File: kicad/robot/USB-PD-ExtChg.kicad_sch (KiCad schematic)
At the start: 28 parts, among them J1 USBC_Receptacle_SMD_RA, Q3 YJL3416A, Q4 YJL3416A, U18 AP33771DKZ-13, U25 TVS0500DRV, U26 TPD1E05U06, U27 TPD1E05U06

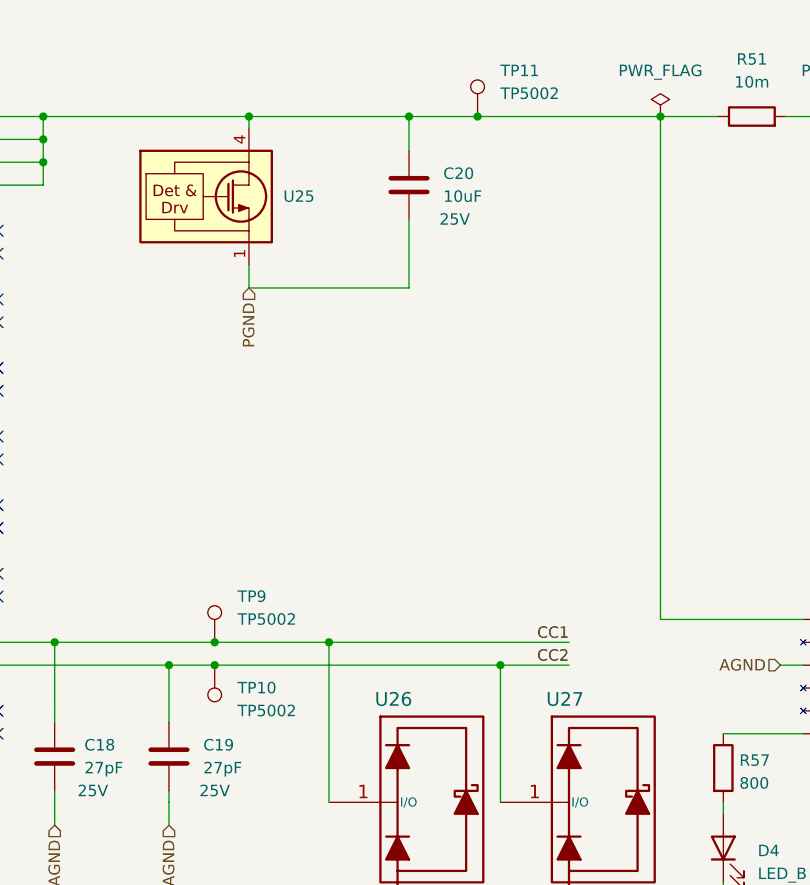
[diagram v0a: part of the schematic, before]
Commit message: Hide all test point values keep ref
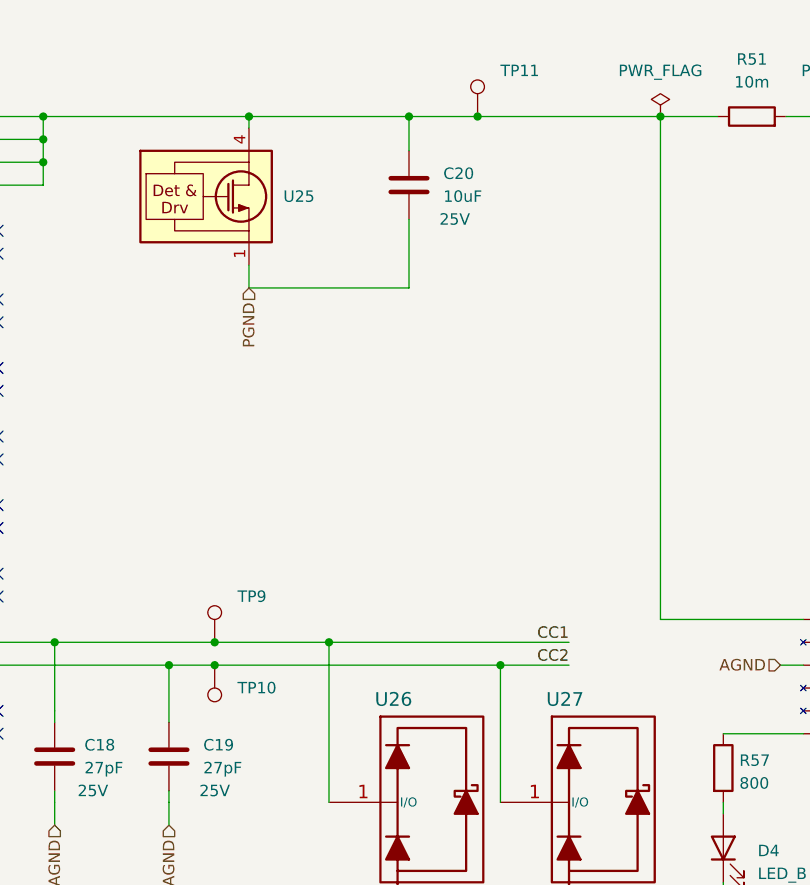
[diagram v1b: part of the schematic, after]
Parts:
- TP10, TP11, TP9: value TP5002 -> TestPoint
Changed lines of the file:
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@@
       (effects (font (size 1.27 1.27)) (justify left))
     )
-    (property "Value" "TP5002" (at 209.55 181.61 0)
-      (effects (font (size 1.27 1.27)) (justify left))
+    (property "Value" "TestPoint" (at 209.55 181.61 0)
+      (effects (font (size 1.27 1.27)) (justify left) hide)
     )
     (property "Footprint" "TestPoint:KEYSTONE_5002" (at 212.09 184.15 0)
@@
       (effects (font (size 1.27 1.27)) (justify left))
     )
-    (property "Value" "TP5002" (at 238.76 123.19 0)
-      (effects (font (size 1.27 1.27)) (justify left))
+    (property "Value" "TestPoint" (at 238.76 123.19 0)
+      (effects (font (size 1.27 1.27)) (justify left) hide)
     )
     (property "Footprint" "TestPoint:KEYSTONE_5002" (at 241.3 125.73 0)
@@
       (effects (font (size 1.27 1.27)) (justify right))
     )
-    (property "Value" "TP5002" (at 209.55 191.77 0)
-      (effects (font (size 1.27 1.27)) (justify right))
+    (property "Value" "TestPoint" (at 209.55 191.77 0)
+      (effects (font (size 1.27 1.27)) (justify right) hide)
     )
     (property "Footprint" "TestPoint:KEYSTONE_5002" (at 201.93 186.69 0)

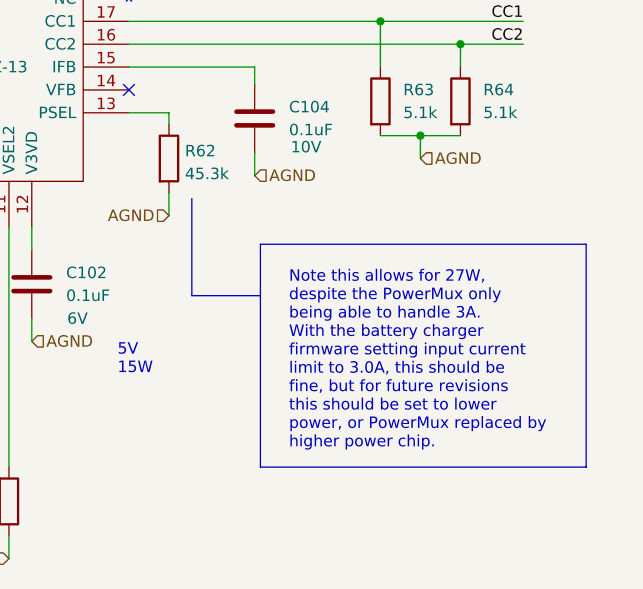
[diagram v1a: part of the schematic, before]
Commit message: Swap out R62 from 45.3k to 16k
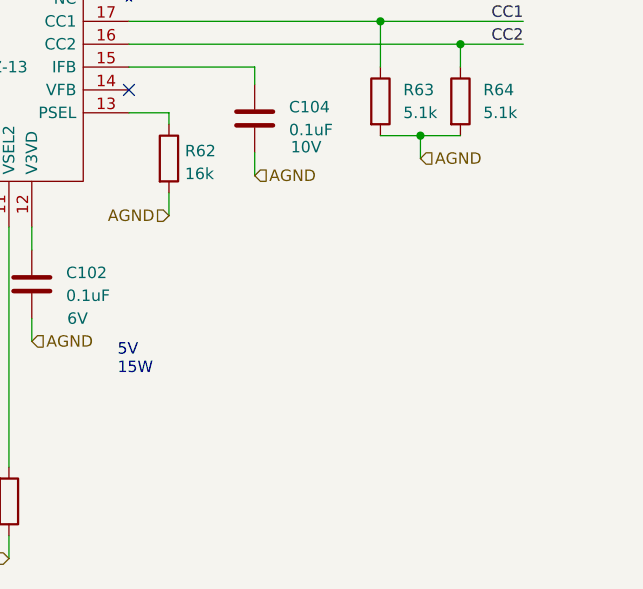
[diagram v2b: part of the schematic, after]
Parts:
- R62: value 45.3k -> 16k; Manufacturer Stackpole Electronics -> (none); Part Number RMCF0603FT45K3 -> (none)
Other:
- note removed: "Note this allows for 27W, despite the PowerMux only being able to handle 3A. With the battery charger firmware setting input current limit to 3.0A, this should be fine, but for future revisions this should be set to lower power, or PowerMux replaced by higher power chip."
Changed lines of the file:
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@@
-    (stroke (width 0) (type default))
-  )
-  (polyline (pts (xy 360.045 233.68) (xy 323.85 233.68))
     (stroke (width 0) (type default))
   )
@@
     (stroke (width 0) (type default))
   )
-  (polyline (pts (xy 323.85 208.915) (xy 360.045 208.915))
-    (stroke (width 0) (type default))
-  )
   (wire (pts (xy 187.96 125.73) (xy 210.82 125.73))
     (stroke (width 0) (type default))
@@
     (stroke (width 0) (type default))
   )
-  (polyline (pts (xy 360.045 208.915) (xy 360.045 233.68))
-    (stroke (width 0) (type default))
-  )
   (wire (pts (xy 263.525 194.31) (xy 272.415 194.31))
     (stroke (width 0) (type default))
@@
     (stroke (width 0) (type default))
   )
-  (polyline (pts (xy 323.85 214.63) (xy 323.85 233.68))
-    (stroke (width 0) (type default))
-  )
   (wire (pts (xy 187.96 133.35) (xy 187.96 130.81))
     (stroke (width 0.254) (type default))
@@
     (stroke (width 0) (type default))
   )
-  (polyline (pts (xy 316.23 203.835) (xy 316.23 214.63))
-    (stroke (width 0) (type default))
-  )
   (wire (pts (xy 228.6 125.73) (xy 228.6 129.54))
     (stroke (width 0) (type default))
@@
     (stroke (width 0.254) (type default))
   )
-  (polyline (pts (xy 323.85 214.63) (xy 323.85 208.915))
-    (stroke (width 0) (type default))
-  )
   (wire (pts (xy 189.23 184.15) (xy 207.01 184.15))
     (stroke (width 0.254) (type default))
@@
     (stroke (width 0) (type default))
   )
-  (polyline (pts (xy 316.23 214.63) (xy 323.85 214.63))
-    (stroke (width 0) (type default))
-  )
   (wire (pts (xy 210.82 125.73) (xy 210.82 127))
     (stroke (width 0) (type default))
@@
   )
   (text "5V\n15W" (at 307.975 223.52 0)
-    (effects (font (size 1.27 1.27)) (justify left bottom))
-  )
-  (text "Note this allows for 27W, \ndespite the PowerMux only\nbeing able to handle 3A.\nWith the battery charger\nfirmware setting input current\nlimit to 3.0A, this should be\nfine, but for future revisions\nthis should be set to lower \npower, or PowerMux replaced by\nhigher power chip."
-    (at 327.025 231.775 0)
     (effects (font (size 1.27 1.27)) (justify left bottom))
   )
@@
       (effects (font (size 1.27 1.27)) (justify left))
     )
-    (property "Value" "45.3k" (at 315.468 201.0922 0)
+    (property "Value" "16k" (at 315.468 201.0922 0)
       (effects (font (size 1.27 1.27)) (justify left))
     )
@@
       (effects (font (size 1.27 1.27)) hide)
     )
-    (property "Manufacturer" "Stackpole Electronics" (at 313.69 199.39 0)
-      (effects (font (size 1.27 1.27)) hide)
-    )
-    (property "Part Number" "RMCF0603FT45K3" (at 313.69 199.39 0)
-      (effects (font (size 1.27 1.27)) hide)
-    )
+    (property "Manufacturer" "" (at 313.69 199.39 0)
+      (effects (font (size 1.27 1.27)) hide)
+    )
+    (property "Part Number" "" (at 313.69 199.39 0)
+      (effects (font (size 1.27 1.27)) hide)
+    )
+    (property "Manufacturer Part Number" "" (at 313.69 199.39 0)
+      (effects (font (size 1.27 1.27)) hide)
+    )
+    (property "Supplier" "" (at 313.69 199.39 0)
+      (effects (font (size 1.27 1.27)) hide)
+    )
+    (property "Supplier Part Number" "" (at 313.69 199.39 0)
+      (effects (font (size 1.27 1.27)) hide)
+    )
+    (property "Populated" "" (at 313.69 199.39 0)
+      (effects (font (size 1.27 1.27)) hide)
+    )
+    (property "ID" "" (at 313.69 199.39 0)
+      (effects (font (size 1.27 1.27)) hide)
+    )

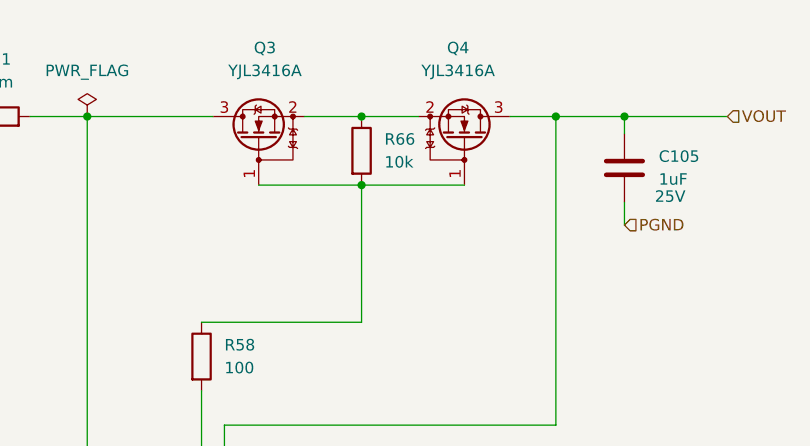
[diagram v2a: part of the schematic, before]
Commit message: Made R66 DNP
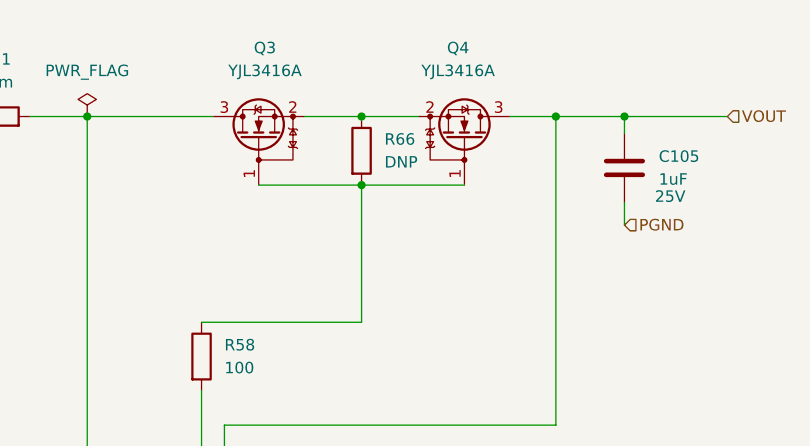
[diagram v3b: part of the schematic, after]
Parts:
- R66: value 10k -> DNP; Manufacturer Stackpole Electronics -> (none); Part Number RMCF0603JT10K0 -> (none)
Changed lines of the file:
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@@
       (effects (font (size 1.27 1.27)) (justify left))
     )
-    (property "Value" "10k" (at 309.88 130.8099 0)
+    (property "Value" "DNP" (at 309.88 130.8099 0)
       (effects (font (size 1.27 1.27)) (justify left))
     )
@@
       (effects (font (size 1.27 1.27)) hide)
     )
-    (property "Manufacturer" "Stackpole Electronics" (at 307.34 129.54 0)
+    (property "Manufacturer" "" (at 307.34 129.54 0)
       (effects (font (size 1.27 1.27)) hide)
     )
-    (property "Part Number" "RMCF0603JT10K0" (at 307.34 129.54 0)
+    (property "Part Number" "" (at 307.34 129.54 0)
       (effects (font (size 1.27 1.27)) hide)
     )

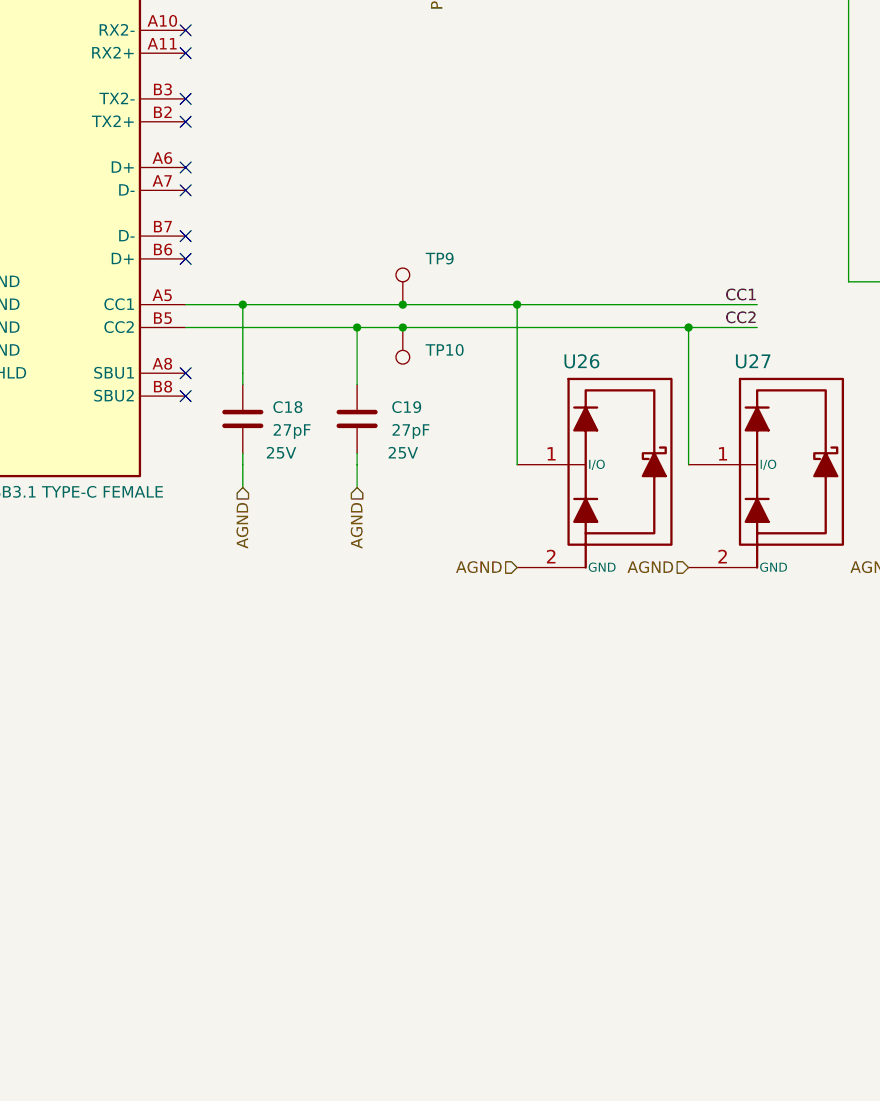
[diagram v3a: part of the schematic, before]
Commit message: Adding switch to connect d+/- from both USB from Pc to pi
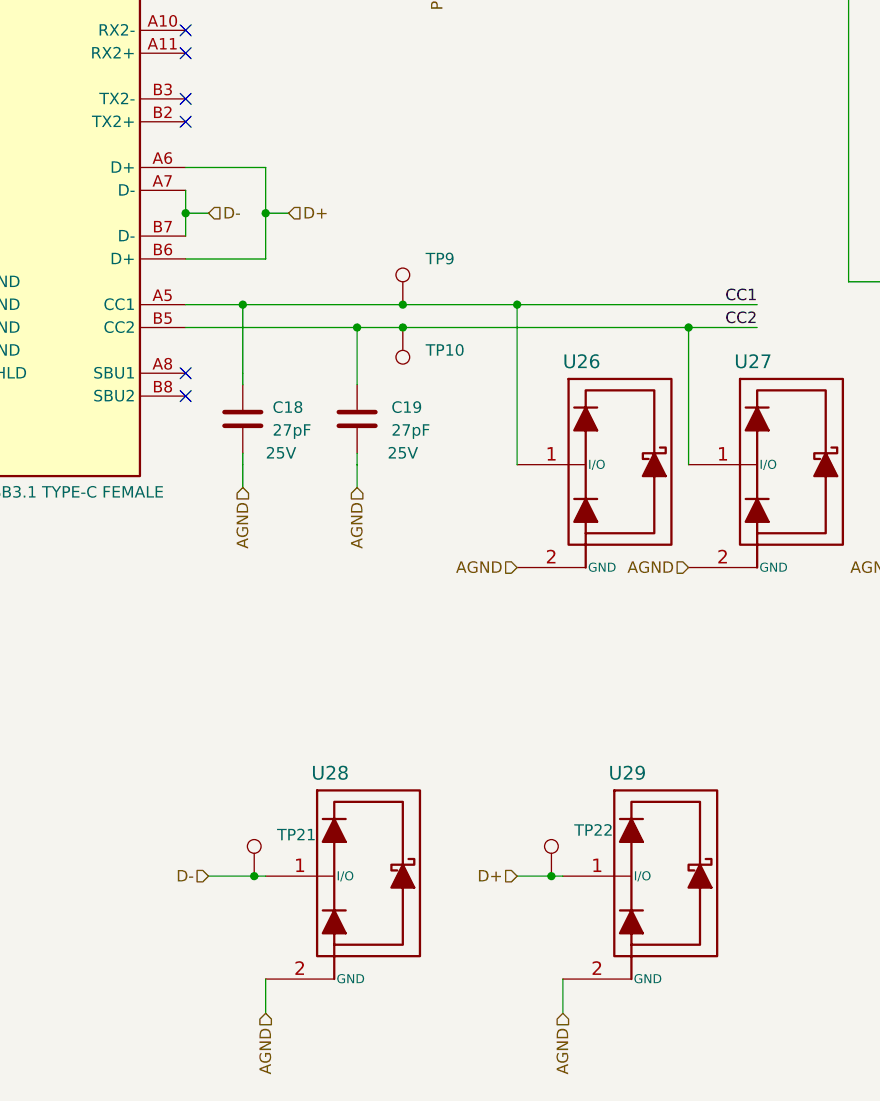
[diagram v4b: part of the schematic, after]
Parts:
- added TP21, TP22: TestPoint, TestPoint:KEYSTONE_5002, symbol Connector:TestPoint
- added U28, U29: TPD1E05U06, Package_X1SON:TPD1E05U06DPYR, symbol Diode:TPD1E05U06
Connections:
- net AGND: now also U28.2 (GND), U29.2 (GND)
- net D+: now reaches J1.A6 (D+)
- net D+: now also J1.B6 (D+), TP22.1, U29.1 (I/O)
- net D-: now reaches J1.A7 (D-)
- net D-: now also J1.B7 (D-), TP21.1, U28.1 (I/O)
- no-connect marks 16 -> 12

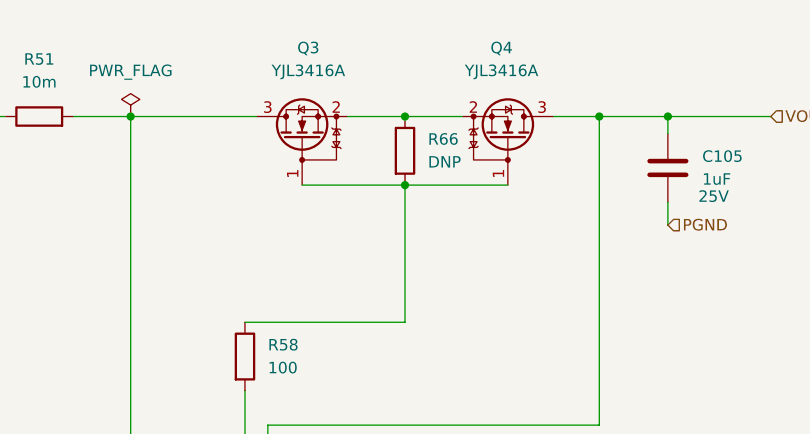
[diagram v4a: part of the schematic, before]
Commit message: Adding DNP bulk capacitance to SYS and Vboost rails. Some populared
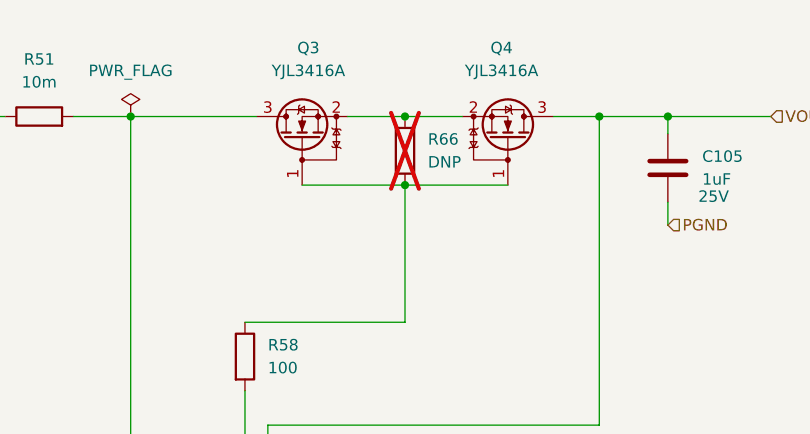
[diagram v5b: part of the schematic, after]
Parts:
- R66: now not fitted; now left out of the parts list
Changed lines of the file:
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@@
   )
   (symbol (lib_id "Device:R") (at 307.34 129.54 0) (unit 1)
-    (in_bom yes) (on_board yes) (dnp no) (fields_autoplaced)
+    (in_bom no) (on_board yes) (dnp yes) (fields_autoplaced)
     (property "Reference" "R66" (at 309.88 128.2699 0)
       (effects (font (size 1.27 1.27)) (justify left))
